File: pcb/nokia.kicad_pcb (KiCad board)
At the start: 4 copper layers, 42.1 x 108 mm, 96 parts, among them J1 Conn_01x07, J2 USB_B_Micro, J20 Conn_01x04_Pin, J3 SM03B-SRSS-TB, J4 Conn_01x06_Pin, J6 SM03B-SRSS-TB, M1 Vibration, Q1 BC847, SW1 SW_Push, U1 W25Q128JVS, U4 NCP1117-3.3_SOT223, U5 RP2350_80QFN, Y1 ABM8-272-T3

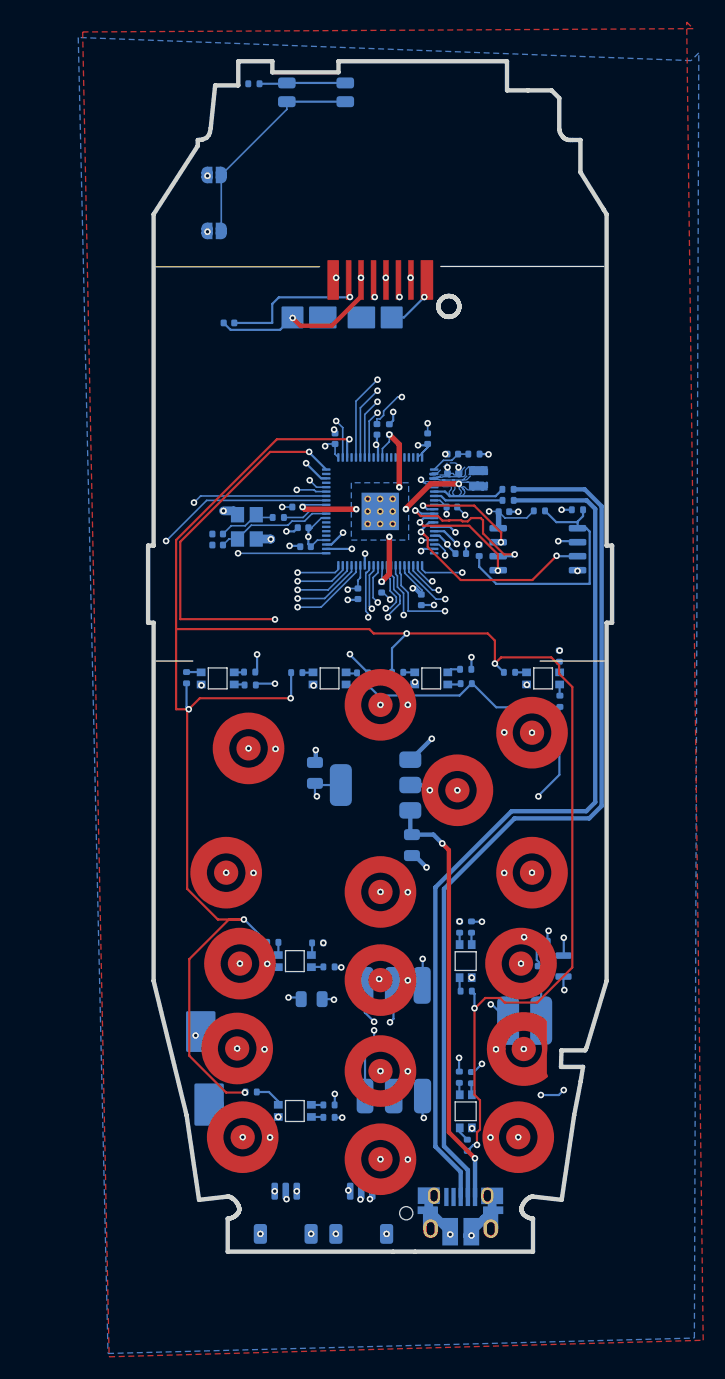
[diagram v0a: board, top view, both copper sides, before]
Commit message: add rtc and gauge, regulator
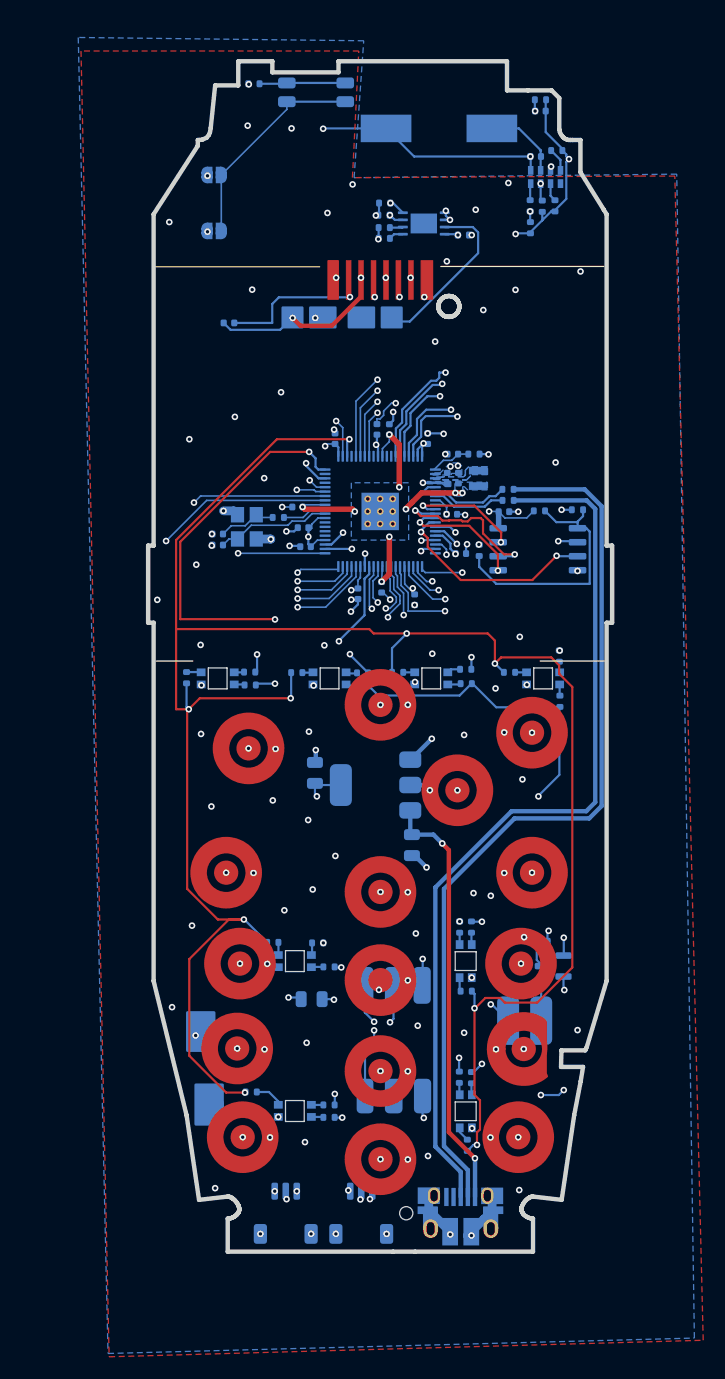
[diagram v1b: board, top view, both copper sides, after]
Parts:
- added C22: 100n, Capacitor_SMD:C_0402_1005Metric, B.Cu at (56.6, 28.0)
- added C23: 100m, 5V5, CoreElectronics_Components:Kemet_FC_10.5X5.5, B.Cu at (47.8, 25.4)
- added C24: 100n, Capacitor_SMD:C_0402_1005Metric, B.Cu at (57.0, 23.9)
- added R33: 10k, Resistor_SMD:R_0402_1005Metric, B.Cu at (42.9, 32.2)
- added R34: 10k, Resistor_SMD:R_0402_1005Metric, B.Cu at (57.2, 32.5)
- added R35: 10k, Resistor_SMD:R_0402_1005Metric, B.Cu at (56.1, 34.5)
- added R36: 10k, Resistor_SMD:R_0402_1005Metric, B.Cu at (58.4, 32.5)
- added R37: 120R, Resistor_SMD:R_0402_1005Metric, B.Cu at (56.1, 32.5)
- added R38: 10k, Resistor_SMD:R_0402_1005Metric, B.Cu at (58.5, 27.5)
- added R39: 100k, Resistor_SMD:R_0402_1005Metric, B.Cu at (57.0, 22.9)
- added R40: 10k, Resistor_SMD:R_0402_1005Metric, B.Cu at (42.8, 33.3)
- added R41: 10k, Resistor_SMD:R_0402_1005Metric, B.Cu at (50.0, 35.1)
- added R42: 47k, Resistor_SMD:R_0402_1005Metric, B.Cu at (42.9, 35.4)
- added R43: 100, Resistor_SMD:R_0402_1005Metric, B.Cu at (42.9, 34.5)
- added U2: LC709203FQH-01TWG, Package_DFN_QFN:WDFN-8-1EP_4x3mm_P0.65mm_EP2.4x1.8mm, B.Cu at (46.5, 34.1)
- added Y2: RV-3028-C7_32.768kHz_1ppm_TA_QC, CoreElectronics_Components:MicroCrystal_RV3028C7, B.Cu at (57.5, 29.9)
- moved C12 0.66 mm to (49.0, 60.5)
- moved C15 0.61 mm to (45.6, 68.2)
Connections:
- J20 pad 1: +3V3 -> Net-(J20-Pin_1)
- J20 pad 3: unconnected-(J20-Pin_3-Pad3) -> Net-(J20-Pin_3)
- L1 pad 1: (no net) -> +1V1
- L1 pad 2: (no net) -> /VREG_LX
- U5 pad 54: /GPIO43_ADC3 -> /ALARMB
- U5 pad 55: /GPIO44_ADC4 -> /SDA0
- U5 pad 56: /GPIO45_ADC5 -> /SCL0
- U5 pad 57: /GPIO46_ADC6 -> /SDA
- U5 pad 58: /GPIO47_ADC7 -> /SCL
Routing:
- net /SCL0: track 0.00 -> 38.9 mm, vias 0 -> 2
- net /SDA0: track 0.00 -> 36.0 mm, vias 0 -> 2
- net /SCL: track 0.00 -> 32.7 mm, vias 0 -> 2
- net GND: track 51.4 -> 82.3 mm, vias 35 -> 93
- net /SDA: track 0.00 -> 29.0 mm, vias 0 -> 2
- net /ALARMB: track 0.00 -> 24.7 mm, vias 0 -> 2
- net Net-(J20-Pin_1): track 0.00 -> 15.5 mm
- net +3V3: track 60.5 -> 75.8 mm, vias 42 -> 47
- net Net-(J20-Pin_3): track 0.00 -> 11.3 mm, vias 0 -> 2
- net Net-(Y2-VBACKUP): track 0.00 -> 7.10 mm
- net +1V1: track 26.5 -> 29.8 mm, vias 8 -> 9
- net /GPIO14: track 38.7 -> 41.2 mm
- net /EVI: track 0.00 -> 2.15 mm
- net /~{INT}: track 0.00 -> 1.67 mm
- net Net-(Y2-SDA): track 0.00 -> 1.45 mm
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
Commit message: first version of pcb with 2350 finished
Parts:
- moved C79 9.21 mm to (37.5, 40.2)
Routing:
- net /GPIO9: track 35.5 -> 21.1 mm
- net /GPIO8: track 47.8 -> 36.0 mm
- net Net-(J1-Pin_7): track 12.5 -> 2.01 mm
- net /GPIO7: track 46.9 -> 36.6 mm
- net /GPIO6: track 55.8 -> 46.0 mm
- net /GPIO16: track 37.3 -> 29.9 mm
- net /GPIO32: track 167.1 -> 159.7 mm
- net /GPIO18: track 56.0 -> 49.7 mm
- net /GPIO17: track 46.8 -> 40.8 mm
- net /GPIO5: track 59.8 -> 55.2 mm
- net +3V3: track 75.8 -> 80.1 mm, vias 47 -> 49
- net GND: track 82.3 -> 78.9 mm, vias 93 -> 96
- net /GPIO19: track 60.0 -> 57.7 mm
- net /GPIO4: track 68.1 -> 66.1 mm
- net +1V1: track 29.8 -> 28.0 mm
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
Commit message: pcb v0.2
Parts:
- removed D2, D3, D4, D5, D6, D7, D8, D9: LED_ARGB, LED_SMD:RGBLED-reverse
- removed J4: Conn_01x06_Pin, Connector:sim connector connector
- removed JP1, JP2: Jumper_2_Open, Jumper:SolderJumper-2_P1.3mm_Open_RoundedPad1.0x1.5mm
- removed R11, R12, R14, R15, R16, R19, R20, R22, R23, R25, R26, R28, R29, R31, R32: 90, Resistor_SMD:R_0402_1005Metric
- removed R13, R18, R21, R24, R27, R30, R4, R5: 140, Resistor_SMD:R_0402_1005Metric
- removed R33, R40, R41: 10k, Resistor_SMD:R_0402_1005Metric
- removed R42: 47k, Resistor_SMD:R_0402_1005Metric
- removed R43: 100, Resistor_SMD:R_0402_1005Metric
- removed U2: LC709203FQH-01TWG, Package_DFN_QFN:WDFN-8-1EP_4x3mm_P0.65mm_EP2.4x1.8mm
- added R44: 3k, Resistor_SMD:R_0402_1005Metric, B.Cu at (30.6, 116.0)
- added R45: 3k, Resistor_SMD:R_0402_1005Metric, B.Cu at (42.5, 118.5)
- added R46: 3k, Resistor_SMD:R_0402_1005Metric, B.Cu at (54.8, 116.3)
- added R47: 3k, Resistor_SMD:R_0402_1005Metric, B.Cu at (55.1, 113.6)
- added R48: 3k, Resistor_SMD:R_0402_1005Metric, B.Cu at (43.9, 113.8)
- added R49: 3k, Resistor_SMD:R_0402_1005Metric, B.Cu at (30.0, 107.9)
- added R50: 3k, Resistor_SMD:R_0402_1005Metric, B.Cu at (29.3, 100.2)
- added R51: 3k, Resistor_SMD:R_0402_1005Metric, B.Cu at (41.2, 101.4)
- added R52: 3k, Resistor_SMD:R_0402_1005Metric, B.Cu at (55.3, 99.7)
- added R53: 3k, Resistor_SMD:R_0402_1005Metric, B.Cu at (28.0, 92.0)
- added R54: 3k, Resistor_SMD:R_0402_1005Metric, B.Cu at (41.0, 89.9)
- added R55: 3k, Resistor_SMD:R_0402_1005Metric, B.Cu at (56.8, 92.0)
- added R56: 3k, Resistor_SMD:R_0402_1005Metric, B.Cu at (42.5, 78.3)
- added R57: 3k, Resistor_SMD:R_0402_1005Metric, B.Cu at (56.9, 80.1)
- added R58: 3k, Resistor_SMD:R_0402_1005Metric, B.Cu at (50.0, 84.5)
- added R59: 3k, Resistor_SMD:R_0402_1005Metric, B.Cu at (30.0, 80.7)
- R6: value 1k -> 3k
- moved C23 82.3 mm to (43.4, 107.6)
- moved R39 74.5 mm to (37.2, 94.7), turned to -90 degrees
- moved C24 73.2 mm to (38.3, 94.7), turned to -90 degrees
- moved C22 69.6 mm to (39.5, 95.5), turned to -90 degrees
- moved R38 68.7 mm to (39.5, 93.5), turned to 90 degrees
- moved Y2 66.6 mm to (41.4, 94.5), turned to -90 degrees
- moved R37 63.6 mm to (44.0, 94.9), turned to 0 degrees
- moved R34 62.1 mm to (48.0, 93.9), turned to 180 degrees
- moved R36 61.3 mm to (48.0, 92.9), turned to 180 degrees
- moved R35 61.0 mm to (48.0, 94.9), turned to 180 degrees
- moved R6 4.03 mm to (32.6, 25.1), turned to 90 degrees
- moved SW1 1.43 mm to (35.3, 28.1)
- moved C19 1.23 mm to (35.0, 104.4)
- moved R17 1.02 mm to (43.9, 73.8)
- moved KP#1 1.00 mm to (55.5, 120.5)
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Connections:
- J20 pad 1: Net-(J20-Pin_1) -> +3V3
- J20 pad 3: Net-(J20-Pin_3) -> unconnected-(J20-Pin_3-Pad3)
- KP#1 pad 1: +3V3 -> GND
- KP*1 pad 1: +3V3 -> GND
- KP0 pad 1: +3V3 -> GND
- KP1 pad 1: +3V3 -> GND
- KP2 pad 1: +3V3 -> GND
- KP3 pad 1: +3V3 -> GND
- KP4 pad 1: +3V3 -> GND
- KP5 pad 1: +3V3 -> GND
- KP6 pad 1: +3V3 -> GND
- KP7 pad 1: +3V3 -> GND
- KP8 pad 1: +3V3 -> GND
- KP9 pad 1: +3V3 -> GND
- KPC1 pad 1: +3V3 -> GND
- KPDOWN1 pad 1: +3V3 -> GND
- KPSELECT1 pad 1: +3V3 -> GND
- KPUP1 pad 1: +3V3 -> GND
- R6 pad 1: Net-(R6-Pad1) -> +3V3
- R6 pad 2: GND -> /GPIO28
- SW1 pad 1: Net-(R6-Pad1) -> GND
- SW1 pad 2: Net-(JP1-A) -> /GPIO28
- U5 pad 35: /RUN -> unconnected-(U5-RUN-Pad35)
- U5 pad 53: /GPIO42_ADC2 -> /~{INT}
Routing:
- net /GPIO32: track 159.7 -> 0.00 mm, vias 8 -> 0
- net /GPIO30: track 147.3 -> 0.00 mm, vias 9 -> 0
- net /GPIO34: track 196.9 -> 54.0 mm, vias 9 -> 2
- net +3V3: track 80.1 -> 210.7 mm, vias 49 -> 25
- net /GPIO22: track 53.4 -> 0.00 mm, vias 2 -> 0
- net /GPIO23: track 52.7 -> 0.00 mm, vias 2 -> 0
- net /GPIO15: track 47.8 -> 0.00 mm, vias 2 -> 0
- net /~{INT}: track 1.67 -> 49.4 mm, vias 0 -> 2
- net /SCL0: track 38.9 -> 0.00 mm, vias 2 -> 0
- net /RUN: track 36.3 -> 0.00 mm, vias 2 -> 0
- net /SDA0: track 36.0 -> 0.00 mm, vias 2 -> 0
- net /ALARMB: track 24.4 -> 0.00 mm, vias 2 -> 0
- net /SCL: track 32.7 -> 56.0 mm
- net /SDA: track 29.0 -> 49.8 mm
- net Net-(JP1-A): track 19.5 -> 0.00 mm
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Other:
- outline, holes or cut-outs redrawn

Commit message: pcb v0.3
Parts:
- removed C22: 100n, Capacitor_SMD:C_0402_1005Metric
- removed J6: SM03B-SRSS-TB, Connector_JST:JST_SH_SM03B-SRSS-TB_1x03-1MP_P1.00mm_Horizontal
- removed R17: 90, Resistor_SMD:R_0402_1005Metric
- added C25: 10u, Capacitor_SMD:C_0805_2012Metric, B.Cu at (50.0, 49.8)
- added C26: 100nF, Capacitor_SMD:C_0805_2012Metric, B.Cu at (26.6, 37.2)
- added C27: 22uF, Capacitor_SMD:C_0805_2012Metric, B.Cu at (26.3, 35.2)
- added C28: 22uF, Capacitor_SMD:C_0805_2012Metric, B.Cu at (26.4, 33.1)
- added C29: 100nF, Capacitor_SMD:C_0805_2012Metric, B.Cu at (25.8, 46.5)
- added C30: 22uF, Capacitor_SMD:C_0805_2012Metric, B.Cu at (27.8, 46.5)
- added C33: 47uF, Capacitor_SMD:C_0805_2012Metric, B.Cu at (53.8, 24.8)
- added C34: 1uF, Capacitor_SMD:C_0805_2012Metric, B.Cu at (26.8, 28.9)
- added C35: 22uF, Capacitor_SMD:C_0805_2012Metric, B.Cu at (29.8, 46.5)
- added D10: BAS16J, Diode_SMD:D_SOD-323F, B.Cu at (46.9, 27.0)
- added D12: SS34, Diode_SMD:D_SMA, B.Cu at (27.8, 51.8)
- added D2: LED, LED_SMD:LED_REVERSE, B.Cu at (27.5, 74.3)
- added D3: LED, LED_SMD:LED_REVERSE, B.Cu at (37.9, 74.3)
- added D4: LED, LED_SMD:LED_REVERSE, B.Cu at (47.1, 74.3)
- added D5: LED, LED_SMD:LED_REVERSE, B.Cu at (34.8, 113.9)
- added D6: LED, LED_SMD:LED_REVERSE, B.Cu at (50.2, 113.3)
- added D7: LED, LED_SMD:LED_REVERSE, B.Cu at (35.0, 100.0)
- added D8: LED, LED_SMD:LED_REVERSE, B.Cu at (50.2, 99.8)
- added D9: LED, LED_SMD:LED_REVERSE, B.Cu at (57.5, 74.4)
- added F1: Polyfuse, Fuse:Fuse_Bourns_MF-SM_7.98x5.44mm, B.Cu at (59.7, 38.0)
- added J5: USB_B_Micro, Connector_USB:USB_Micro-B_Molex_47346-0001, B.Cu at (38.2, 123.8)
- added JP2: Jumper_2_Open, Jumper:SolderJumper-2_P1.3mm_Open_RoundedPad1.0x1.5mm, B.Cu at (36.8, 38.0)
- added L2: 4.7uH, Inductor_SMD:L_Neosid_MicroCoil_Ms36-L, B.Cu at (34.6, 30.0)
- added Q2: BC847, Package_TO_SOT_SMD:SOT-23, B.Cu at (31.5, 73.6)
- added Q4: BSS138, Package_TO_SOT_SMD:SOT-23, B.Cu at (42.5, 22.4)
- added Q5: BC847, Package_TO_SOT_SMD:SOT-23, B.Cu at (53.1, 113.7)
- added Q6: BSS138, Package_TO_SOT_SMD:SOT-23, B.Cu at (56.3, 29.2)
- added Q7: BC847, Package_TO_SOT_SMD:SOT-23, B.Cu at (47.1, 99.9)
- added Q9: BC847, Package_TO_SOT_SMD:SOT-23, B.Cu at (53.2, 73.5)
- added R11: 220, Resistor_SMD:R_0402_1005Metric, B.Cu at (36.7, 98.3)
- added R12: 220, Resistor_SMD:R_0402_1005Metric, B.Cu at (48.1, 97.5)
- added R13: 220, Resistor_SMD:R_0402_1005Metric, B.Cu at (56.7, 72.5)
- added R14: 1K, Resistor_SMD:R_0402_1005Metric, B.Cu at (45.2, 21.8)
- added R15: 100k, Resistor_SMD:R_0402_1005Metric, B.Cu at (59.4, 33.1)
- added R16: 1K, Resistor_SMD:R_0402_1005Metric, B.Cu at (59.8, 29.9)
- added R18: 100, Resistor_SMD:R_0402_1005Metric, B.Cu at (53.3, 27.4)
- added R19: 1K, Resistor_SMD:R_0402_1005Metric, B.Cu at (55.1, 31.8)
- added R20: 10k, Resistor_SMD:R_0402_1005Metric, B.Cu at (55.1, 33.0)
- added R21: 200k, Resistor_SMD:R_0402_1005Metric, B.Cu at (53.3, 26.4)
- added R22: 1K, Resistor_SMD:R_0402_1005Metric, B.Cu at (30.4, 23.9)
- added R4: 220, Resistor_SMD:R_0402_1005Metric, B.Cu at (28.9, 72.7)
- added R41: 1K, Resistor_SMD:R_0402_1005Metric, B.Cu at (27.2, 44.2)
- added R5: 220, Resistor_SMD:R_0402_1005Metric, B.Cu at (36.5, 72.7)
- added SW2: SW_Push, Button_Switch_SMD:SW_SPST_PTS810, B.Cu at (56.9, 35.9)
- added TP1: TestPoint, TestPoint:TestPoint_THTPad_D1.5mm_Drill0.7mm, F.Cu at (24.6, 54.4)
- added TP2: TestPoint, TestPoint:TestPoint_THTPad_D1.5mm_Drill0.7mm, F.Cu at (24.4, 51.0)
- added U2: NCP1117-3.3_SOT223, Package_TO_SOT_SMD:SOT-223-3_TabPin2, B.Cu at (57.5, 50.4)
- added U3: TP5400, Package_SO:SOIC-8_3.9x4.9mm_P1.27mm, B.Cu at (27.5, 40.9)
- added U6: 74LVC1G14, Package_TO_SOT_SMD:SOT-23-5_HandSoldering, B.Cu at (40.6, 33.0)
- added U7: 74LVC1G17, Package_TO_SOT_SMD:SOT-23-5_HandSoldering, B.Cu at (42.9, 26.1)
- added U8: 74LVC1G175, Package_TO_SOT_SMD:TSOT-23-6_HandSoldering, B.Cu at (48.9, 22.9)
- C1: value 10u -> 22uF
- C23: value 100m, 5V5 -> 10u; footprint CoreElectronics_Components:Kemet_FC_10.5X5.5 -> Capacitor_SMD:C_0805_2012Metric
- C5: value 10u -> 100n; footprint Capacitor_SMD:C_0805_2012Metric -> Capacitor_SMD:C_0402_1005Metric
- J2: value USB_B_Micro -> Conn_02x04_Counter_Clockwise; footprint Connector_USB:USB_Micro-B_Amphenol_10103594-0001LF_Horizontal -> Connector_PinHeader_2.54mm:PinHeader_2x04_P2.54mm_Vertical_SMD
- J3: value SM03B-SRSS-TB -> Conn_01x02_Pin; footprint Connector_JST:JST_SH_SM03B-SRSS-TB_1x03-1MP_P1.00mm_Horizontal -> Connector_PinHeader_1.00mm:PinHeader_1x02_P1.00mm_Vertical_SMD_Pin1Left; moved to F.Cu
- R1: value DNF -> 10k
- R10: value 0 -> 220
- R6: value 3k -> 220
- R9: value DNF -> 220
- U4: value NCP1117-3.3_SOT223 -> SIL2308; footprint Package_TO_SOT_SMD:SOT-223-3_TabPin2 -> Package_TO_SOT_SMD:SOT-23-6
- moved J3 95.9 mm to (42.6, 28.0), turned to 0 degrees
- moved J2 90.3 mm to (48.3, 33.9), turned to 90 degrees
- moved C23 61.6 mm to (50.0, 46.4), turned to -90 degrees
- moved C1 55.2 mm to (30.9, 37.2), turned to 180 degrees
- moved R9 53.5 mm to (36.9, 115.2), turned to 180 degrees
- moved R10 51.9 mm to (52.4, 111.3), turned to 180 degrees
- moved R6 50.2 mm to (48.5, 72.7), turned to 180 degrees
- moved U4 44.6 mm to (57.7, 43.2)
- moved C5 11.9 mm to (39.5, 95.5), turned to -90 degrees
- moved Q1 6.63 mm to (56.9, 95.0)
- moved R47 3.27 mm to (56.4, 110.6), turned to -90 degrees
- moved D1 2.36 mm to (55.3, 97.8), turned to 90 degrees
- moved M1 2.33 mm to (55.5, 111.3)
- moved R37 1.60 mm to (44.0, 96.5)
- moved R8 1.60 mm to (55.7, 58.2)
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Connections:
- C1 pad 2: GND -> -BATT
- C10 pad 2: GND -> -BATT
- C11 pad 2: GND -> -BATT
- C12 pad 2: GND -> -BATT
- C13 pad 2: GND -> -BATT
- C14 pad 2: GND -> -BATT
- C15 pad 2: GND -> -BATT
- C16 pad 2: GND -> -BATT
- C17 pad 2: GND -> -BATT
- C18 pad 2: GND -> -BATT
- C19 pad 2: GND -> -BATT
- C2 pad 2: GND -> -BATT
- C20 pad 2: GND -> -BATT
- C21 pad 2: GND -> -BATT
- C23 pad 1: Net-(Y2-VBACKUP) -> Net-(U2-VI)
- C23 pad 2: GND -> -BATT
- C24 pad 2: GND -> -BATT
- C3 pad 2: GND -> -BATT
- C4 pad 2: GND -> -BATT
- C5 pad 1: +3V3 -> Net-(Y2-VBACKUP)
- C5 pad 2: GND -> -BATT
- C6 pad 2: GND -> -BATT
- C7 pad 2: GND -> -BATT
- C79 pad 1: GND -> -BATT
- C8 pad 2: GND -> -BATT
- C9 pad 2: GND -> -BATT
- J1 pad 6: GND -> -BATT
- J2 pad 1: VBUS -> -BATT
- J2 pad 2: /USB_D- -> /SWCLK
- J2 pad 3: /USB_D+ -> -BATT
- J2 pad 4: unconnected-(J2-ID-Pad4) -> /SWD
- J2 pad 5: GND -> /GPIO0
- J2 pad 6: GND -> -BATT
- J20 pad 1: +3V3 -> +BATT
- J20 pad 4: GND -> -BATT
- J3 pad 1: /GPIO1 -> /GPIO34
- J3 pad 2: GND -> -BATT
- KP#1 pad 1: GND -> -BATT
- KP*1 pad 1: GND -> -BATT
- KP0 pad 1: GND -> -BATT
- KP1 pad 1: GND -> -BATT
- KP2 pad 1: GND -> -BATT
- KP3 pad 1: GND -> -BATT
- KP4 pad 1: GND -> -BATT
- KP5 pad 1: GND -> -BATT
- KP6 pad 1: GND -> -BATT
- KP7 pad 1: GND -> -BATT
- KP8 pad 1: GND -> -BATT
- KP9 pad 1: GND -> -BATT
- KPC1 pad 1: GND -> -BATT
- KPDOWN1 pad 1: GND -> -BATT
- KPSELECT1 pad 1: GND -> -BATT
- KPUP1 pad 1: GND -> -BATT
- LS2 pad 2: GND -> -BATT
- Q1 pad 2: GND -> -BATT
- R1 pad 1: +3V3 -> /QSPI_SS
- R1 pad 2: /FLASH_SS -> Net-(R1-Pad2)
- R10 pad 1: /QSPI_SS -> Net-(Q5-C)
- R10 pad 2: /FLASH_SS -> Net-(D6-K)
- R39 pad 2: GND -> -BATT
- R6 pad 1: +3V3 -> Net-(Q9-C)
- R6 pad 2: /GPIO28 -> Net-(D4-K)
- R9 pad 1: /GPIO0 -> Net-(Q5-C)
- R9 pad 2: /FLASH_SS -> Net-(D5-K)
- SW1 pad 1: GND -> -BATT
- SW1 pad 2: /GPIO28 -> /Btn
- U1 pad 1: /FLASH_SS -> /QSPI_SS
- U1 pad 4: GND -> -BATT
- U4 pad 1: GND -> Net-(R16-Pad2)
- U4 pad 2: +3V3 -> Net-(F1-Pad1)
- U4 pad 3: VBUS -> Net-(R15-Pad1)
- U5 pad 22: /GPIO22 -> unconnected-(U5-GPIO22-Pad22)
- U5 pad 23: /GPIO23 -> unconnected-(U5-GPIO23-Pad23)
- U5 pad 25: /GPIO24 -> unconnected-(U5-GPIO24-Pad25)
- U5 pad 26: /GPIO25 -> unconnected-(U5-GPIO25-Pad26)
- U5 pad 27: /GPIO26 -> unconnected-(U5-GPIO26-Pad27)
- U5 pad 28: /GPIO27 -> unconnected-(U5-GPIO27-Pad28)
- U5 pad 36: /GPIO28 -> /Btn
- U5 pad 37: /GPIO29 -> unconnected-(U5-GPIO29-Pad37)
- U5 pad 38: /GPIO30 -> unconnected-(U5-GPIO30-Pad38)
- U5 pad 39: /GPIO31 -> unconnected-(U5-GPIO31-Pad39)
- U5 pad 40: /GPIO32 -> unconnected-(U5-GPIO32-Pad40)
- U5 pad 44: /GPIO35 -> /Push
- U5 pad 49: /GPIO40_ADC0 -> unconnected-(U5-GPIO40_ADC0-Pad49)
- U5 pad 52: /GPIO41_ADC1 -> unconnected-(U5-GPIO41_ADC1-Pad52)
- U5 pad 54: /ALARMB -> unconnected-(U5-GPIO43_ADC3-Pad54)
- U5 pad 55: /SDA0 -> unconnected-(U5-GPIO44_ADC4-Pad55)
- U5 pad 56: /SCL0 -> unconnected-(U5-GPIO45_ADC5-Pad56)
- U5 pad 62: GND -> -BATT
- U5 pad 80: /GPIO3 -> unconnected-(U5-GPIO3-Pad80)
- U5 pad 81: GND -> -BATT
- Y1 pad 2: GND -> -BATT
- Y1 pad 4: GND -> -BATT
- Y2 pad 1: /CLK -> unconnected-(Y2-CLKOUT-Pad1)
- Y2 pad 5: GND -> -BATT
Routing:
- net -BATT: track 0.00 -> 292.2 mm, vias 0 -> 84
- net /GPIO15: track 0.00 -> 101.8 mm, vias 0 -> 3
- net +5V: track 0.00 -> 88.9 mm, vias 0 -> 10
- net /Btn: track 0.00 -> 86.6 mm, vias 0 -> 5
- net VBUS: track 39.8 -> 123.4 mm, vias 2 -> 3
- net GND: track 69.8 -> 0.00 mm, vias 86 -> 0
- net /Push: track 0.00 -> 66.8 mm, vias 0 -> 2
- net /GPIO1: track 84.8 -> 30.3 mm
- net /GPIO0: track 94.7 -> 50.5 mm, vias 3 -> 2
- net /GPIO28: track 43.1 -> 0.00 mm
- net /SWD: track 83.2 -> 41.8 mm, vias 2 -> 3
- net /SWCLK: track 83.0 -> 46.8 mm
- net Net-(R1-Pad2): track 0.00 -> 32.9 mm, vias 0 -> 2
- net +BATT: track 0.00 -> 31.2 mm, vias 0 -> 2
- net Net-(D12-A): track 0.00 -> 28.4 mm, vias 0 -> 2
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- added copper zone on B.Cu, net -BATT
- added copper zone on F.Cu, net -BATT
- added copper zone on In2.Cu, net -BATT
- removed copper zone on B.Cu, net GND
- removed copper zone on F.Cu, net GND
- removed copper zone on In2.Cu, net GND
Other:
- outline, holes or cut-outs redrawn
